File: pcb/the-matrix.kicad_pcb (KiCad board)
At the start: 2 copper layers, 102 x 102 mm, 81 parts, among them J1 DNP, J2 DNP, J3 Conn_02x20_Odd_Even, J4 Conn_02x20_Odd_Even, J5 Conn_02x20_Odd_Even, J6 Conn_02x20_Odd_Even, Q1 Q_PMOS_GDS, Q10 Q_PMOS_GDS, Q11 Q_PMOS_GDS, Q12 Q_PMOS_GDS, Q13 Q_PMOS_GDS, Q14 Q_PMOS_GDS, Q15 Q_PMOS_GDS, Q16 Q_PMOS_GDS, Q17 Q_PMOS_GDS, Q18 Q_PMOS_GDS, Q19 Q_PMOS_GDS, Q2 Q_PMOS_GDS, Q20 Q_PMOS_GDS, Q21 Q_PMOS_GDS, Q22 Q_PMOS_GDS, Q23 Q_PMOS_GDS, Q24 Q_PMOS_GDS, Q25 Q_PMOS_GDS, Q26 Q_PMOS_GDS, Q27 Q_PMOS_GDS, Q28 Q_PMOS_GDS, Q29 Q_PMOS_GDS, Q3 Q_PMOS_GDS, Q30 Q_PMOS_GDS, Q31 Q_PMOS_GDS, Q32 Q_PMOS_GDS, Q33 Q_PMOS_GDS, Q34 Q_PMOS_GDS, Q35 Q_PMOS_GDS, Q36 Q_PMOS_GDS, Q37 Q_PMOS_GDS, Q38 Q_PMOS_GDS, Q39 Q_PMOS_GDS, Q4 Q_PMOS_GDS, Q40 Q_PMOS_GDS, Q5 Q_PMOS_GDS, Q6 Q_PMOS_GDS, Q7 Q_PMOS_GDS, Q8 Q_PMOS_GDS, Q9 Q_PMOS_GDS, U1 74HC595, U10 TPIC6B595N, U2 74HC595, U3 74HC595, U4 74HC595, U5 74HC595, U6 TPIC6B595N, U7 TPIC6B595N, U8 TPIC6B595N, U9 TPIC6B595N

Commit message: one more session for today
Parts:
- Q1, Q10, Q11, Q12, Q13, Q14, Q15, Q16, Q17, Q18, Q19, Q2, Q20, Q21, Q22, Q23, Q24, Q25, Q26, Q27, Q28, Q29, Q3, Q30, Q31, Q32, Q33, Q34, Q35, Q36, Q37, Q38, Q39, Q4, Q40, Q5, Q6, Q7, Q8, Q9: footprint Package_TO_SOT_THT:TO-220-3_Vertical -> Package_TO_SOT_THT:TO-251-3_Vertical
- moved U5 372.0 mm to (189.1, 37.4), turned to -90 degrees
- moved U4 361.9 mm to (189.3, 119.4), turned to -90 degrees
- moved Q40 355.0 mm to (203.3, 54.0)
- moved U9 352.5 mm to (182.0, 79.2)
- moved U8 344.3 mm to (182.1, 52.3)
- moved U10 343.2 mm to (161.9, 78.9)
- moved Q39 333.1 mm to (185.5, 41.0), turned to 90 degrees
- moved Q32 330.5 mm to (199.0, 110.8), turned to 0 degrees
- moved Q38 316.7 mm to (181.2, 45.9), turned to 0 degrees
- moved U7 313.6 mm to (161.9, 52.4)
- moved Q37 313.2 mm to (197.5, 65.5), turned to -90 degrees
- moved J2 307.1 mm to (145.9, 44.0), turned to -90 degrees
- moved Q30 304.0 mm to (194.5, 106.0), turned to -90 degrees
- moved Q31 303.4 mm to (185.5, 128.2), turned to 90 degrees
- moved Q36 301.1 mm to (194.2, 61.5), turned to -90 degrees
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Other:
- copper layers 2 -> 4
- board text added: "the matrix v1 rivques 2025"

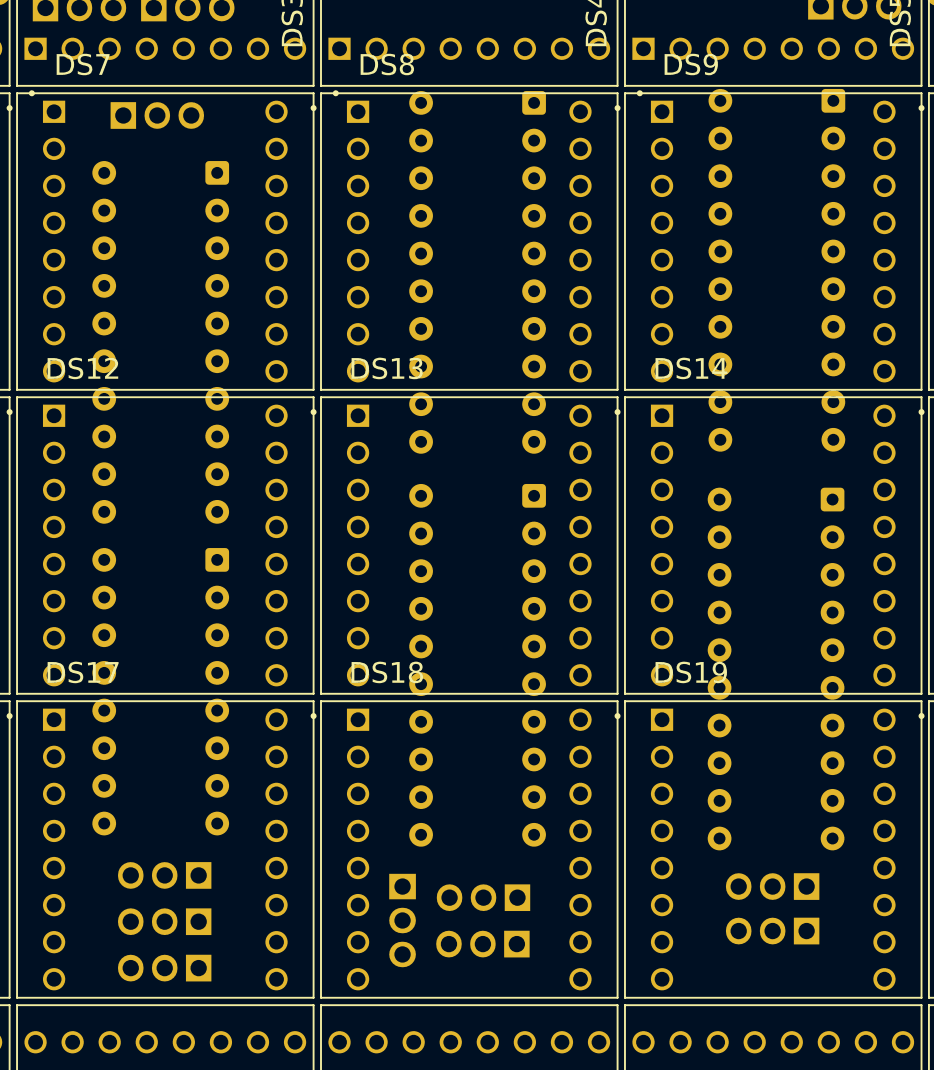
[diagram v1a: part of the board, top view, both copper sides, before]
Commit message: it is not in fact cheaper from digikey
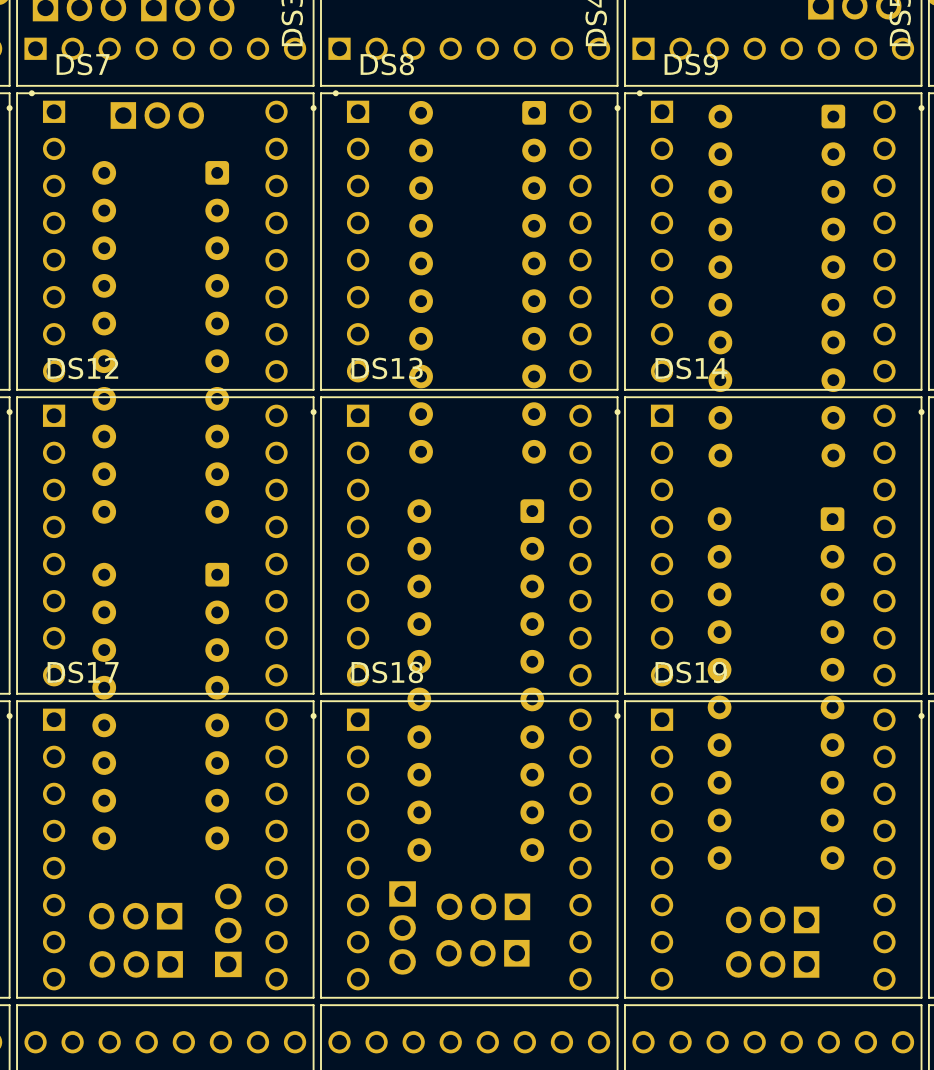
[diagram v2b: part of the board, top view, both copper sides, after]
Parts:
- moved Q23 3.46 mm to (137.3, 110.5)
- moved Q24 3.38 mm to (137.3, 107.2)
- moved Q18 2.25 mm to (180.2, 110.5)
- moved Q19 2.25 mm to (180.2, 107.5)
- moved Q22 2.02 mm to (141.2, 110.5), turned to 90 degrees
- moved U9 1.32 mm to (182.0, 80.5)
- moved U8 1.06 mm to (182.1, 53.3)
- moved U10 1.04 mm to (161.8, 79.9)
- moved U3 1.00 mm to (140.5, 84.2)
- moved U7 0.67 mm to (161.9, 53.1)
- moved Q20 0.62 mm to (160.7, 109.8)
- moved Q21 0.62 mm to (160.8, 106.6)
- moved Q17 0.50 mm to (153.0, 105.8)
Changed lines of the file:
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@@
 	(footprint "Package_TO_SOT_THT:TO-251-3_Vertical"
 		(layer "B.Cu")
-		(at 139.25 110.75 180)
+		(at 141.25 110.5 90)
 		(descr "TO-251-3, Vertical, RM 2.29mm, IPAK, see https://www.diodes.com/assets/Package-Files/TO251.pdf, generated with kicad-footprint-generator TO_SOT_THT_generate.py")
 		(tags "TO-251-3 Vertical RM 2.29mm IPAK")
 		(property "Reference" "Q22"
-			(at 2.29 2.22 0)
+			(at 2.29 2.22 90)
 			(layer "B.SilkS")
 			(effects
@@
 		)
 		(property "Value" "Q_PMOS_GDS"
-			(at 2.29 -1.98 0)
+			(at 2.29 -1.98 90)
 			(layer "B.Fab")
 			(effects
@@
 		)
 		(property "Datasheet" ""
-			(at 0 0 0)
+			(at 0 0 90)
 			(layer "B.Fab")
 			(hide yes)
@@
 		)
 		(property "Description" "P-MOSFET transistor, gate/drain/source"
-			(at 0 0 0)
+			(at 0 0 90)
 			(layer "B.Fab")
 			(hide yes)
@@
 		(attr through_hole)
 		(fp_line
-			(start 5.69 1.38)
-			(end 5.69 1.16)
+			(start 3.409 -1.14)
+			(end 3.461 -1.14)
 			(stroke
 				(width 0.12)
@@
 		)
 		(fp_line
-			(start 3.409 -1.14)
-			(end 3.461 -1.14)
+			(start 5.69 1.38)
+			(end 5.69 1.16)
 			(stroke
 				(width 0.12)
@@
 		(fp_line
 			(start -1.11 1.38)
-			(end 5.69 1.38)
+			(end -1.11 1.16)
 			(stroke
 				(width 0.12)
@@
 		(fp_line
 			(start -1.11 1.38)
-			(end -1.11 1.16)
+			(end 5.69 1.38)
 			(stroke
 				(width 0.12)
@@
 		)
 		(fp_text user "${REFERENCE}"
-			(at 2.29 0.12 0)
+			(at 2.29 0.12 90)
 			(layer "B.Fab")
 			(effects
@@
 		)
 		(pad "1" thru_hole rect
-			(at 0 0 180)
+			(at 0 0 90)
 			(size 1.7175 1.8)
 			(drill 1.1)
@@
 		)
 		(pad "2" thru_hole oval
-			(at 2.29 0 180)
+			(at 2.29 0 90)
 			(size 1.7175 1.8)
 			(drill 1.1)
@@
 		)
 		(pad "3" thru_hole oval
-			(at 4.58 0 180)
+			(at 4.58 0 90)
 			(size 1.7175 1.8)
 			(drill 1.1)
@@
 	(footprint "Package_DIP:DIP-16_W7.62mm"
 		(layer "B.Cu")
-		(at 140.5 83.22 180)
+		(at 140.5 84.22 180)
 		(descr "16-lead though-hole mounted DIP package, row spacing 7.62mm (300 mils)")
 		(tags "THT DIP DIL PDIP 2.54mm 7.62mm 300mil")
@@
 	(footprint "Package_TO_SOT_THT:TO-251-3_Vertical"
 		(layer "B.Cu")
-		(at 153 105.25 -90)
+		(at 153 105.75 -90)
 		(descr "TO-251-3, Vertical, RM 2.29mm, IPAK, see https://www.diodes.com/assets/Package-Files/TO251.pdf, generated with kicad-footprint-generator TO_SOT_THT_generate.py")
 		(tags "TO-251-3 Vertical RM 2.29mm IPAK")
@@
 	(footprint "Package_TO_SOT_THT:TO-251-3_Vertical"
 		(layer "B.Cu")
-		(at 160.75 106 180)
+		(at 160.75 106.62 180)
 		(descr "TO-251-3, Vertical, RM 2.29mm, IPAK, see https://www.diodes.com/assets/Package-Files/TO251.pdf, generated with kicad-footprint-generator TO_SOT_THT_generate.py")
 		(tags "TO-251-3 Vertical RM 2.29mm IPAK")
@@
 	(footprint "Package_TO_SOT_THT:TO-251-3_Vertical"
 		(layer "B.Cu")
-		(at 139.25 104.5 180)
+		(at 137.29 107.25 180)
 		(descr "TO-251-3, Vertical, RM 2.29mm, IPAK, see https://www.diodes.com/assets/Package-Files/TO251.pdf, generated with kicad-footprint-generator TO_SOT_THT_generate.py")
 		(tags "TO-251-3 Vertical RM 2.29mm IPAK")
@@
 	(footprint "Package_DIP:DIP-20_W7.62mm"
 		(layer "B.Cu")
-		(at 182.055 52.26 180)
+		(at 182.055 53.32 180)
 		(descr "20-lead though-hole mounted DIP package, row spacing 7.62mm (300 mils)")
 		(tags "THT DIP DIL PDIP 2.54mm 7.62mm 300mil")
@@
 	(footprint "Package_DIP:DIP-20_W7.62mm"
 		(layer "B.Cu")
-		(at 182 79.15 180)
+		(at 182 80.47 180)
 		(descr "20-lead though-hole mounted DIP package, row spacing 7.62mm (300 mils)")
 		(tags "THT DIP DIL PDIP 2.54mm 7.62mm 300mil")
@@
 		(sheetname "/")
 		(sheetfile "the-matrix.kicad_sch")
-		(attr through_hole)
+		(attr through_hole dnp)
 		(fp_line
 			(start -1.38 1.38)
@@
 	(footprint "Package_DIP:DIP-20_W7.62mm"
 		(layer "B.Cu")
-		(at 161.87 78.9 180)
+		(at 161.75 79.93 180)
 		(descr "20-lead though-hole mounted DIP package, row spacing 7.62mm (300 mils)")
 		(tags "THT DIP DIL PDIP 2.54mm 7.62mm 300mil")
@@
 	(footprint "Package_DIP:DIP-20_W7.62mm"
 		(layer "B.Cu")
-		(at 161.87 52.4 180)
+		(at 161.87 53.07 180)
 		(descr "20-lead though-hole mounted DIP package, row spacing 7.62mm (300 mils)")
 		(tags "THT DIP DIL PDIP 2.54mm 7.62mm 300mil")
@@
 	(footprint "Package_TO_SOT_THT:TO-251-3_Vertical"
 		(layer "B.Cu")
-		(at 180.25 108.25 180)
+		(at 180.25 110.5 180)
 		(descr "TO-251-3, Vertical, RM 2.29mm, IPAK, see https://www.diodes.com/assets/Package-Files/TO251.pdf, generated with kicad-footprint-generator TO_SOT_THT_generate.py")
 		(tags "TO-251-3 Vertical RM 2.29mm IPAK")
@@
 		(sheetname "/")
 		(sheetfile "the-matrix.kicad_sch")
-		(attr through_hole)
+		(attr through_hole dnp)
 		(fp_line
 			(start 1.38 -1.27)
@@
 	(footprint "Package_TO_SOT_THT:TO-251-3_Vertical"
 		(layer "B.Cu")
-		(at 160.71 109.13 180)
+		(at 160.71 109.75 180)
 		(descr "TO-251-3, Vertical, RM 2.29mm, IPAK, see https://www.diodes.com/assets/Package-Files/TO251.pdf, generated with kicad-footprint-generator TO_SOT_THT_generate.py")
 		(tags "TO-251-3 Vertical RM 2.29mm IPAK")
@@
 	(footprint "Package_TO_SOT_THT:TO-251-3_Vertical"
 		(layer "B.Cu")
-		(at 180.25 105.25 180)
+		(at 180.25 107.5 180)
 		(descr "TO-251-3, Vertical, RM 2.29mm, IPAK, see https://www.diodes.com/assets/Package-Files/TO251.pdf, generated with kicad-footprint-generator TO_SOT_THT_generate.py")
 		(tags "TO-251-3 Vertical RM 2.29mm IPAK")
@@
 	(footprint "Package_TO_SOT_THT:TO-251-3_Vertical"
 		(layer "B.Cu")
-		(at 139.25 107.62 180)
+		(at 137.33 110.5 180)
 		(descr "TO-251-3, Vertical, RM 2.29mm, IPAK, see https://www.diodes.com/assets/Package-Files/TO251.pdf, generated with kicad-footprint-generator TO_SOT_THT_generate.py")
 		(tags "TO-251-3 Vertical RM 2.29mm IPAK")

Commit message: an amount of progress on routing
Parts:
- Q1, Q10, Q11, Q12, Q13, Q14, Q15, Q16, Q17, Q18, Q19, Q2, Q20, Q21, Q22, Q23, Q24, Q25, Q26, Q27, Q28, Q29, Q3, Q30, Q31, Q32, Q33, Q34, Q35, Q36, Q37, Q38, Q39, Q4, Q40, Q5, Q6, Q7, Q8, Q9: footprint Package_TO_SOT_THT:TO-251-3_Vertical -> TO-251-ThinPads:TO-251-3_Vertical_ThinPads
- moved U10 0.63 mm to (161.1, 79.9)
- moved U7 0.63 mm to (161.2, 53.1)
- moved U8 0.31 mm to (181.8, 53.3)
- moved U9 0.25 mm to (181.8, 80.5)
- turned DS1 to -90 degrees
- turned DS2 to -90 degrees
- turned DS3 to -90 degrees
- turned DS4 to -90 degrees
- turned DS5 to -90 degrees
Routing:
- net /COLA36: track 0.00 -> 128.9 mm
- net /COLA33: track 0.00 -> 127.8 mm, vias 0 -> 1
- net /COLA34: track 0.00 -> 111.1 mm
- net /COLA35: track 0.00 -> 96.6 mm, vias 0 -> 2
- net /COLA37: track 0.00 -> 92.7 mm
- net /ROWA31: track 0.00 -> 91.9 mm
- net /COLA32: track 0.00 -> 89.6 mm, vias 0 -> 1
- net /ROWA13: track 0.00 -> 88.5 mm
- net /ROWA10: track 0.00 -> 88.0 mm
- net /ROWA18: track 0.00 -> 87.7 mm
- net /ROWA26: track 0.00 -> 87.6 mm
- net /ROWA11: track 0.00 -> 87.1 mm
- net /ROWA19: track 0.00 -> 87.1 mm
- net /ROWA21: track 0.00 -> 87.1 mm
- net /ROWA16: track 0.00 -> 86.8 mm
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
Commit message: route the matrix
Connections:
- J3 pad 1: /COLA0 -> /COLA38
- J3 pad 10: /COLA9 -> /COLA31
- J3 pad 11: /COLA10 -> /COLA28
- J3 pad 12: /COLA11 -> /COLA29
- J3 pad 13: /COLA12 -> /COLA26
- J3 pad 14: /COLA13 -> /COLA27
- J3 pad 15: /COLA14 -> /COLA24
- J3 pad 16: /COLA15 -> /COLA25
- J3 pad 17: /COLA16 -> /COLA22
- J3 pad 18: /COLA17 -> /COLA23
- J3 pad 19: /COLA18 -> /COLA20
- J3 pad 2: /COLA1 -> /COLA39
- J3 pad 20: /COLA19 -> /COLA21
- J3 pad 21: /COLA20 -> /COLA18
- J3 pad 22: /COLA21 -> /COLA19
- J3 pad 23: /COLA22 -> /COLA16
- J3 pad 24: /COLA23 -> /COLA17
- J3 pad 25: /COLA24 -> /COLA14
- J3 pad 26: /COLA25 -> /COLA15
- J3 pad 27: /COLA26 -> /COLA12
- J3 pad 28: /COLA27 -> /COLA13
- J3 pad 29: /COLA28 -> /COLA10
- J3 pad 3: /COLA2 -> /COLA36
- J3 pad 30: /COLA29 -> /COLA11
- J3 pad 31: /COLA30 -> /COLA8
- J3 pad 32: /COLA31 -> /COLA9
- J3 pad 33: /COLA32 -> /COLA6
- J3 pad 34: /COLA33 -> /COLA7
- J3 pad 35: /COLA34 -> /COLA4
- J3 pad 36: /COLA35 -> /COLA5
- J3 pad 37: /COLA36 -> /COLA2
- J3 pad 38: /COLA37 -> /COLA3
- J3 pad 39: /COLA38 -> /COLA0
- J3 pad 4: /COLA3 -> /COLA37
- J3 pad 40: /COLA39 -> /COLA1
- J3 pad 5: /COLA4 -> /COLA34
- J3 pad 6: /COLA5 -> /COLA35
- J3 pad 7: /COLA6 -> /COLA32
- J3 pad 8: /COLA7 -> /COLA33
- J3 pad 9: /COLA8 -> /COLA30
- J6 pad 1: /COLA1 -> /COLA39
- J6 pad 10: /COLA8 -> /COLA30
- J6 pad 11: /COLA11 -> /COLA29
- J6 pad 12: /COLA10 -> /COLA28
- J6 pad 13: /COLA13 -> /COLA27
- J6 pad 14: /COLA12 -> /COLA26
- J6 pad 15: /COLA15 -> /COLA25
- J6 pad 16: /COLA14 -> /COLA24
- J6 pad 17: /COLA17 -> /COLA23
- J6 pad 18: /COLA16 -> /COLA22
- J6 pad 19: /COLA19 -> /COLA21
- J6 pad 2: /COLA0 -> /COLA38
- J6 pad 20: /COLA18 -> /COLA20
- J6 pad 21: /COLA21 -> /COLA19
- J6 pad 22: /COLA20 -> /COLA18
- J6 pad 23: /COLA23 -> /COLA17
- J6 pad 24: /COLA22 -> /COLA16
- J6 pad 25: /COLA25 -> /COLA15
- J6 pad 26: /COLA24 -> /COLA14
- J6 pad 27: /COLA27 -> /COLA13
- J6 pad 28: /COLA26 -> /COLA12
- J6 pad 29: /COLA29 -> /COLA11
- J6 pad 3: /COLA3 -> /COLA37
- J6 pad 30: /COLA28 -> /COLA10
- J6 pad 31: /COLA31 -> /COLA9
- J6 pad 32: /COLA30 -> /COLA8
- J6 pad 33: /COLA33 -> /COLA7
- J6 pad 34: /COLA32 -> /COLA6
- J6 pad 35: /COLA35 -> /COLA5
- J6 pad 36: /COLA34 -> /COLA4
- J6 pad 37: /COLA37 -> /COLA3
- J6 pad 38: /COLA36 -> /COLA2
- J6 pad 39: /COLA39 -> /COLA1
- J6 pad 4: /COLA2 -> /COLA36
- J6 pad 40: /COLA38 -> /COLA0
- J6 pad 5: /COLA5 -> /COLA35
- J6 pad 6: /COLA4 -> /COLA34
- J6 pad 7: /COLA7 -> /COLA33
- J6 pad 8: /COLA6 -> /COLA32
- J6 pad 9: /COLA9 -> /COLA31
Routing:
- net /COLA9: track 0.00 -> 119.5 mm
- net /COLA18: track 0.00 -> 118.5 mm, vias 0 -> 1
- net /COLA4: track 0.00 -> 118.2 mm
- net /COLA10: track 0.00 -> 117.3 mm
- net /COLA20: track 0.00 -> 115.4 mm, vias 0 -> 1
- net /COLA17: track 0.00 -> 113.9 mm
- net /COLA1: track 0.00 -> 112.7 mm, vias 0 -> 1
- net /COLA2: track 0.00 -> 110.5 mm, vias 0 -> 2
- net /ROWA34: track 0.00 -> 109.1 mm
- net /ROWA37: track 0.00 -> 101.5 mm
- net /ROWA5: track 0.00 -> 100.9 mm
- net /COLA12: track 0.00 -> 99.3 mm
- net /ROWA32: track 0.00 -> 96.0 mm
- net /ROWA2: track 0.00 -> 95.6 mm
- net /COLA7: track 0.00 -> 95.2 mm, vias 0 -> 1
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
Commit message: more routing!
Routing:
- net /COLA22: track 91.7 -> 137.4 mm, vias 0 -> 2
- net /COLA17: track 113.9 -> 158.5 mm, vias 0 -> 2
- net /COLA21: track 79.1 -> 121.9 mm, vias 0 -> 2
- net /COLA23: track 90.3 -> 133.1 mm, vias 1 -> 2
- net /COLA35: track 96.6 -> 136.1 mm, vias 2 -> 5
- net /COLA4: track 118.2 -> 157.2 mm, vias 0 -> 2
- net /COLA3: track 85.4 -> 124.0 mm
- net /COLA39: track 85.3 -> 122.1 mm, vias 1 -> 2
- net /COLA32: track 89.6 -> 123.8 mm, vias 1 -> 3
- net /COLA33: track 127.8 -> 161.5 mm
- net /COLA37: track 92.7 -> 126.1 mm, vias 0 -> 2
- net /COLA2: track 110.5 -> 140.6 mm, vias 2 -> 3
- net /COLA18: track 118.5 -> 148.0 mm, vias 1 -> 2
- net /COLA36: track 128.9 -> 157.9 mm
- net /COLA34: track 111.1 -> 139.9 mm, vias 0 -> 2
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
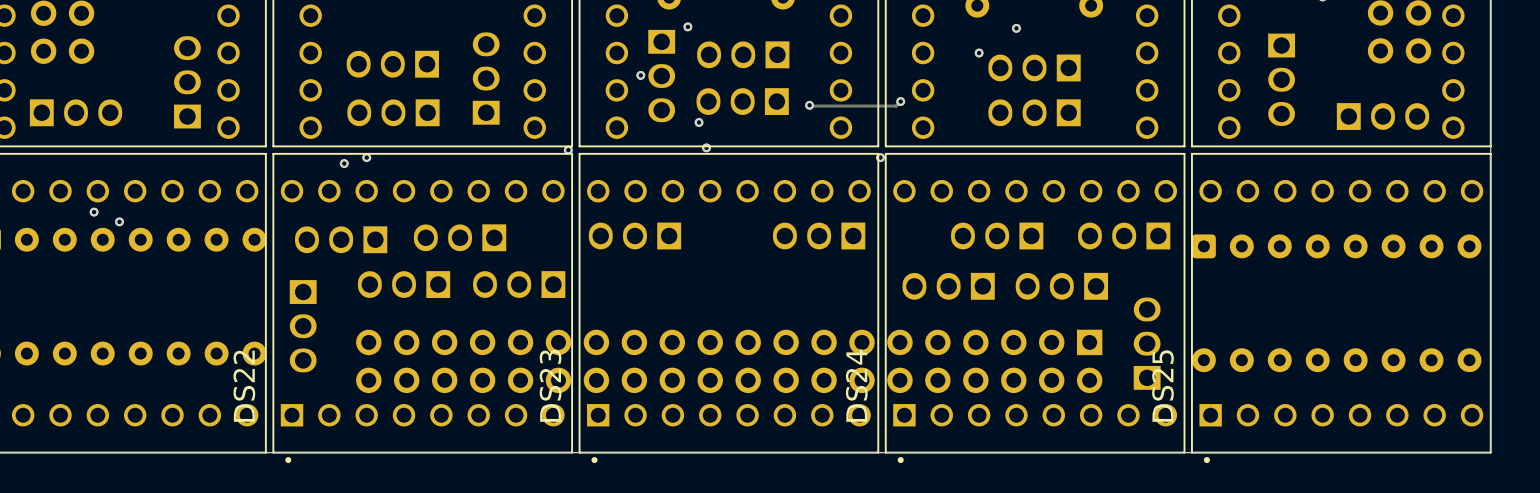
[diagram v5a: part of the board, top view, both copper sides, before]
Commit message: column connectors wired
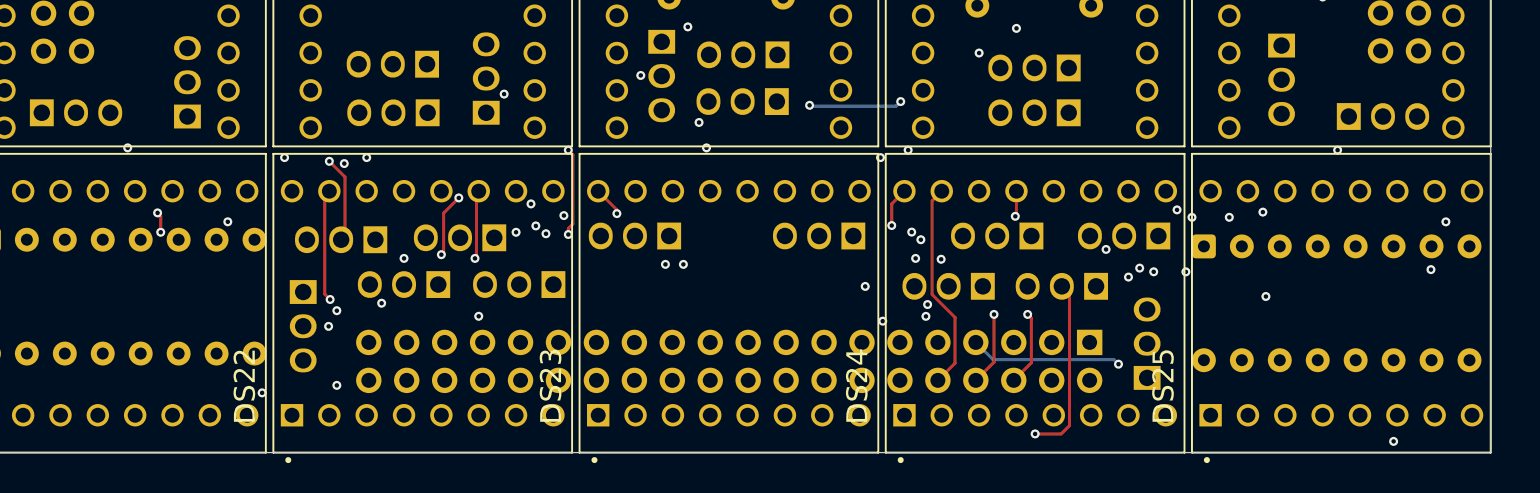
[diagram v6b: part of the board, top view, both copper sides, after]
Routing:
- net /COLA31: track 105.3 -> 152.3 mm, vias 2 -> 5
- net /COLA13: track 106.9 -> 145.9 mm, vias 1 -> 3
- net /COLA37: track 126.1 -> 163.3 mm, vias 2 -> 4
- net /COLA35: track 136.1 -> 172.8 mm, vias 5 -> 7
- net /COLA15: track 106.1 -> 138.0 mm, vias 2 -> 4
- net /COLA6: track 117.5 -> 149.1 mm, vias 3 -> 5
- net /COLA32: track 123.8 -> 155.2 mm, vias 3 -> 5
- net /COLA24: track 106.0 -> 135.1 mm, vias 2 -> 5
- net /COLA0: track 109.9 -> 138.5 mm
- net /COLA33: track 161.5 -> 189.5 mm, vias 1 -> 2
- net /COLA12: track 119.1 -> 146.4 mm, vias 1 -> 3
- net /COLA30: track 107.4 -> 134.3 mm, vias 1 -> 3
- net /COLA36: track 157.9 -> 184.8 mm, vias 0 -> 1
- net /COLA5: track 99.2 -> 125.8 mm, vias 2 -> 3
- net /COLA4: track 157.2 -> 183.7 mm
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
